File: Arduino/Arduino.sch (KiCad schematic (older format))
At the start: 8 parts, among them P1 Power, P2 Analog, P3 Digital, P4 Digital, P5 CONN_01X01, P6 CONN_01X01, P7 CONN_01X01, P8 CONN_01X01

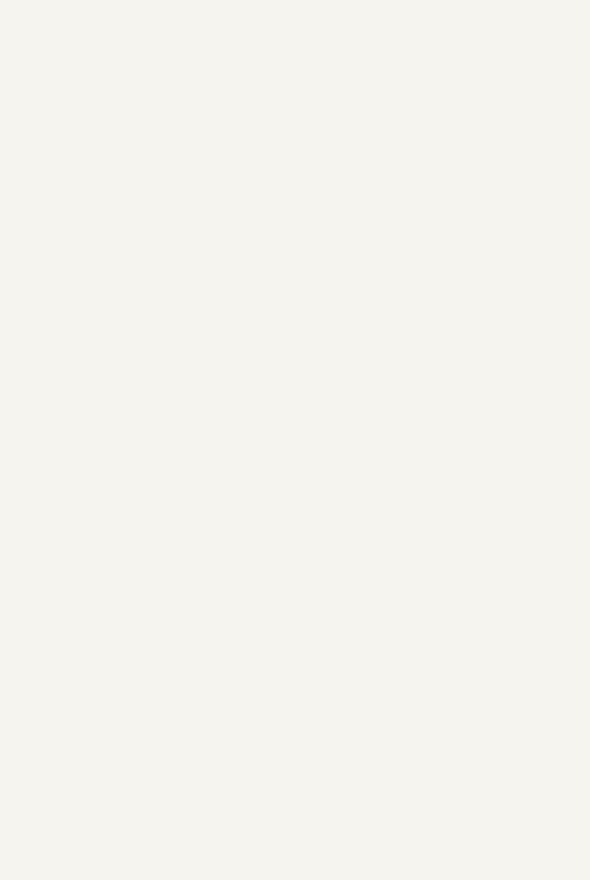
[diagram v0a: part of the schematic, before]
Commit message: Add main processor
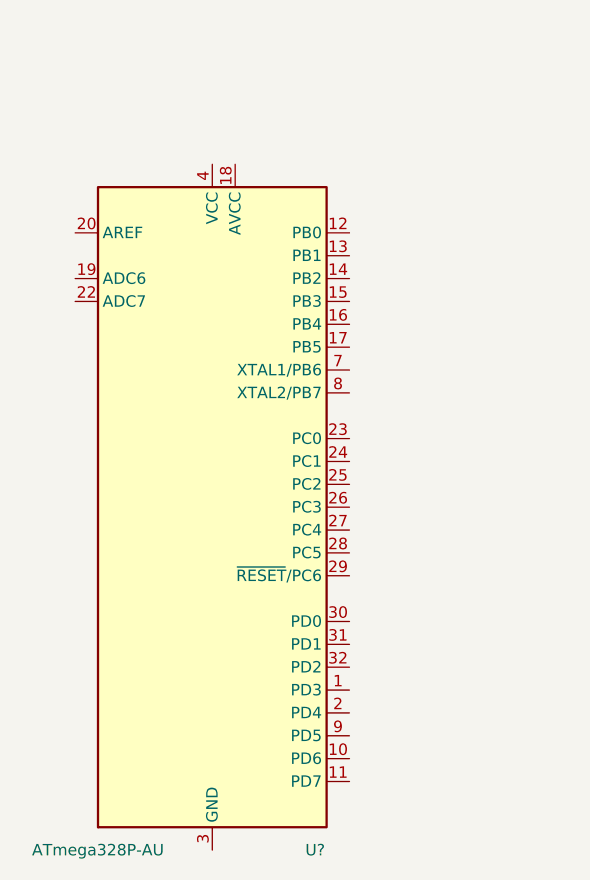
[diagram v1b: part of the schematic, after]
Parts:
- added U?: ATmega328P-AU, Package_QFP:TQFP-32_7x7mm_P0.8mm, symbol MCU_Microchip_ATmega:ATmega328P-AU
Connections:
- new net: U?.21 (GND), U?.3 (GND), U?.5 (GND)
- new net: U?.4 (VCC), U?.6 (VCC)
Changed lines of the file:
@@
 EESchema Schematic File Version 4
-LIBS:Arduino_As_Uno-cache
-EELAYER 26 0
+LIBS:Arduino-cache
+EELAYER 29 0
 EELAYER END
 $Descr A4 11693 8268
@@
 Wire Notes Line
 	10700 1000 10700 500
+$Comp
+L MCU_Microchip_ATmega:ATmega328P-AU U?
+U 1 1 5FF0B667
+P 5900 5000
+F 0 "U?" H 6350 3500 50  0000 C CNN
+F 1 "ATmega328P-AU" H 5400 3500 50  0000 C CNN
+F 2 "Package_QFP:TQFP-32_7x7mm_P0.8mm" H 5900 5000 50  0001 C CIN
+F 3 "http://ww1.microchip.com/downloads/en/DeviceDoc/ATmega328_P%20AVR%20MCU%20with%20picoPower%20Technology%20Data%20Sheet%2040001984A.pdf" H 5900 5000 50  0001 C CNN
+F 4 "ATMEGA328P-AU-ND" H 5900 5000 50  0001 C CNN "Digikey"
+F 5 "C14877" H 5900 5000 50  0001 C CNN "JLC"
+	1    5900 5000
+	1    0    0    -1
+$EndComp
 $EndSCHEMATC
